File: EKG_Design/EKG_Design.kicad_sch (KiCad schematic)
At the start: 0 parts

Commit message: Started EKG-Details and ECG-PulseDetection Circuit Symbols implemented
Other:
- company: (none) -> HAWK
- title: (none) -> EKG-Verstärker
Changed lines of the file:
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@@
 	(generator_version "10.0")
 	(paper "A4")
+	(title_block
+		(title "EKG-Verstärker")
+		(date "2026-04-20")
+		(company "HAWK")
+		(comment 1 "PCB Design SS2026")
+		(comment 2 "M.Mousa")
+		(comment 3 "T. Brown")
+	)
 	(text "Sheet 02 -->"
 		(exclude_from_sim no)

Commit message: Finished EKG Schematic
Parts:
- added H101, H102, H103, H104: MountingHole_Pad, symbol Mechanical:MountingHole_Pad
- added PCB101: Printed Circuit Board (PCB), symbol CustomSymbols:PCB
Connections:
- new net GND: H101.1, H102.1, H103.1, H104.1
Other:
- note added: "Changes, Modifications V1.0 Intial Revision Input Voltage +/- 5V"
- note added: "Date 03.05.2026"
- note added: "Name T.Brown M.Mousa"
- note added: "Rev. 1.0"
- note added: "Revision History"
- note added: "Sheet 01 --> Info"

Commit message: Updated AM Receiver Schematic with all Symbols. Footprint, manifest and data sheet still needed
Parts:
- H101, H102, H103, H104: now left out of the parts list
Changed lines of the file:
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@@
 		(body_style 1)
 		(exclude_from_sim no)
-		(in_bom yes)
-		(on_board yes)
+		(in_bom no)
+		(on_board no)
 		(in_pos_files yes)
 		(dnp yes)
@@
 		(exclude_from_sim no)
 		(in_bom yes)
-		(on_board yes)
+		(on_board no)
 		(in_pos_files yes)
 		(dnp yes)
@@
 		(body_style 1)
 		(exclude_from_sim no)
-		(in_bom yes)
-		(on_board yes)
+		(in_bom no)
+		(on_board no)
 		(in_pos_files yes)
 		(dnp yes)
@@
 		(body_style 1)
 		(exclude_from_sim no)
-		(in_bom yes)
-		(on_board yes)
+		(in_bom no)
+		(on_board no)
 		(in_pos_files yes)
 		(dnp yes)
@@
 		(body_style 1)
 		(exclude_from_sim no)
-		(in_bom yes)
-		(on_board yes)
+		(in_bom no)
+		(on_board no)
 		(in_pos_files yes)
 		(dnp yes)

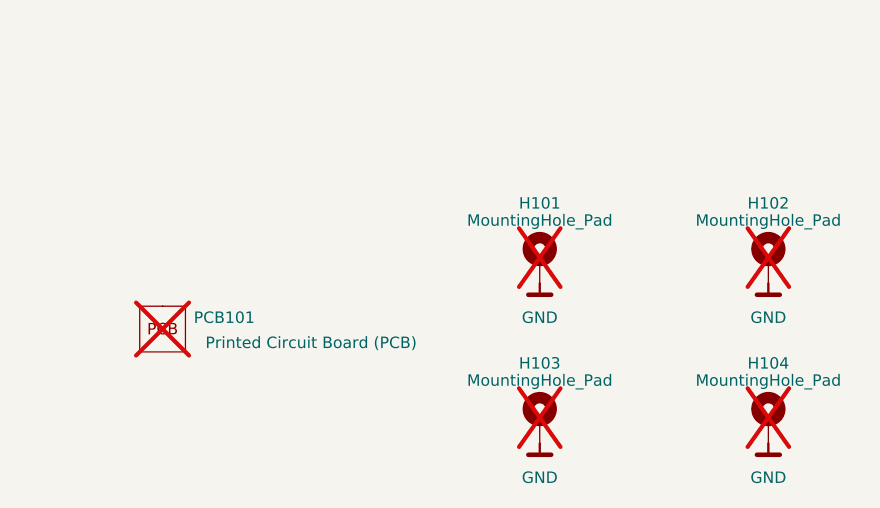
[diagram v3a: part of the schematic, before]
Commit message: Finished ECG Schematic and finished laying out the PCB
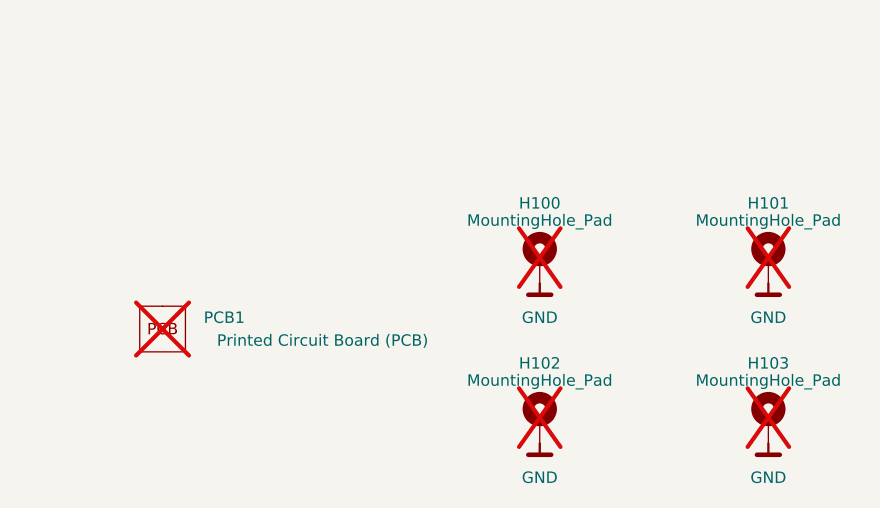
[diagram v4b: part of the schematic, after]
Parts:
- H100: renamed from H101; footprint (none) -> MountingHole:MountingHole_2.2mm_M2_Pad
- H101: renamed from H102; footprint (none) -> MountingHole:MountingHole_2.2mm_M2_Pad
- H102: renamed from H103; footprint (none) -> MountingHole:MountingHole_2.2mm_M2_Pad
- H103: renamed from H104; footprint (none) -> MountingHole:MountingHole_2.2mm_M2_Pad
- renumbered PCB101 to PCB1
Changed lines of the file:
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@@
 		(exclude_from_sim no)
 		(in_bom no)
-		(on_board no)
+		(on_board yes)
 		(in_pos_files yes)
 		(dnp yes)
-		(property "Reference" "H101"
+		(property "Reference" "H100"
 			(at 228.6 129.54 0)
 			(show_name no)
@@
 			)
 		)
-		(property "Footprint" ""
+		(property "Footprint" "MountingHole:MountingHole_2.2mm_M2_Pad"
 			(at 228.6 135.89 0)
 			(hide yes)
@@
 			(project "EKG_Design"
 				(path "/145a8612-0e2a-4b7d-8919-051e741c5f83"
-					(reference "H101")
+					(reference "H100")
 					(unit 1)
 				)
@@
 		(in_pos_files yes)
 		(dnp yes)
-		(property "Reference" "PCB101"
+		(property "Reference" "PCB1"
 			(at 193.548 142.24 0)
 			(show_name no)
@@
 		)
 		(property "Value" "Printed Circuit Board (PCB)"
-			(at 203.2 145.034 0)
+			(at 204.47 144.78 0)
 			(show_name no)
 			(do_not_autoplace no)
@@
 			(project "EKG_Design"
 				(path "/145a8612-0e2a-4b7d-8919-051e741c5f83"
-					(reference "PCB101")
+					(reference "PCB1")
 					(unit 1)
 				)
@@
 		(exclude_from_sim no)
 		(in_bom no)
-		(on_board no)
+		(on_board yes)
+		(in_pos_files yes)
+		(dnp yes)
+		(property "Reference" "H101"
+			(at 254 129.54 0)
+			(show_name no)
+			(do_not_autoplace no)
+			(effects
+				(font
+					(size 1.27 1.27)
+				)
+			)
+		)
+		(property "Value" "MountingHole_Pad"
+			(at 254 131.445 0)
+			(show_name no)
+			(do_not_autoplace no)
+			(effects
+				(font
+					(size 1.27 1.27)
+				)
+			)
+		)
+		(property "Footprint" "MountingHole:MountingHole_2.2mm_M2_Pad"
+			(at 254 135.89 0)
+			(hide yes)
+			(show_name no)
+			(do_not_autoplace no)
+			(effects
+				(font
+					(size 1.27 1.27)
+				)
+			)
+		)
+		(property "Datasheet" ""
+			(at 254 135.89 0)
+			(hide yes)
+			(show_name no)
+			(do_not_autoplace no)
+			(effects
+				(font
+					(size 1.27 1.27)
+				)
+			)
+		)
+		(property "Description" "Mounting Hole with connection"
+			(at 254 135.89 0)
+			(hide yes)
+			(show_name no)
+			(do_not_autoplace no)
+			(effects
+				(font
+					(size 1.27 1.27)
+				)
+			)
+		)
+		(pin "1"
+		)
+		(instances
+			(project "EKG_Design"
+				(path "/145a8612-0e2a-4b7d-8919-051e741c5f83"
+					(reference "H101")
+					(unit 1)
+				)
+			)
+		)
+	)
+	(symbol
+		(lib_id "Mechanical:MountingHole_Pad")
+		(at 228.6 153.67 0)
+		(unit 1)
+		(body_style 1)
+		(exclude_from_sim no)
+		(in_bom no)
+		(on_board yes)
 		(in_pos_files yes)
 		(dnp yes)
 		(property "Reference" "H102"
-			(at 254 129.54 0)
-			(show_name no)
-			(do_not_autoplace no)
-			(effects
-				(font
-					(size 1.27 1.27)
-				)
-			)
-		)
-		(property "Value" "MountingHole_Pad"
-			(at 254 131.445 0)
-			(show_name no)
-			(do_not_autoplace no)
-			(effects
-				(font
-					(size 1.27 1.27)
-				)
-			)
-		)
-		(property "Footprint" ""
-			(at 254 135.89 0)
-			(hide yes)
-			(show_name no)
-			(do_not_autoplace no)
-			(effects
-				(font
-					(size 1.27 1.27)
-				)
-			)
-		)
-		(property "Datasheet" ""
-			(at 254 135.89 0)
-			(hide yes)
-			(show_name no)
-			(do_not_autoplace no)
-			(effects
-				(font
-					(size 1.27 1.27)
-				)
-			)
-		)
-		(property "Description" "Mounting Hole with connection"
-			(at 254 135.89 0)
-			(hide yes)
-			(show_name no)
-			(do_not_autoplace no)
-			(effects
-				(font
-					(size 1.27 1.27)
-				)
-			)
-		)
-		(pin "1"
-		)
-		(instances
-			(project "EKG_Design"
-				(path "/145a8612-0e2a-4b7d-8919-051e741c5f83"
-					(reference "H102")
-					(unit 1)
-				)
-			)
-		)
-	)
-	(symbol
-		(lib_id "Mechanical:MountingHole_Pad")
-		(at 228.6 153.67 0)
-		(unit 1)
-		(body_style 1)
-		(exclude_from_sim no)
-		(in_bom no)
-		(on_board no)
-		(in_pos_files yes)
-		(dnp yes)
-		(property "Reference" "H103"
 			(at 228.6 147.32 0)
 			(show_name no)
@@
 			)
 		)
-		(property "Footprint" ""
+		(property "Footprint" "MountingHole:MountingHole_2.2mm_M2_Pad"
 			(at 228.6 153.67 0)
 			(hide yes)
@@
 			(project "EKG_Design"
 				(path "/145a8612-0e2a-4b7d-8919-051e741c5f83"
-					(reference "H103")
+					(reference "H102")
 					(unit 1)
 				)
@@
 		(exclude_from_sim no)
 		(in_bom no)
-		(on_board no)
+		(on_board yes)
 		(in_pos_files yes)
 		(dnp yes)
-		(property "Reference" "H104"
+		(property "Reference" "H103"
 			(at 254 147.32 0)
 			(show_name no)
@@
 			)
 		)
-		(property "Footprint" ""
+		(property "Footprint" "MountingHole:MountingHole_2.2mm_M2_Pad"
 			(at 254 153.67 0)
 			(hide yes)
@@
 			(project "EKG_Design"
 				(path "/145a8612-0e2a-4b7d-8919-051e741c5f83"
-					(reference "H104")
-					(unit 1)
-				)
+					(reference "H103")
+					(unit 1)
+				)
